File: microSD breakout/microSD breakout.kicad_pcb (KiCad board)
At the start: 2 copper layers, 17.1 x 17.8 mm, 4 parts, among them J1 Micro_SD_Card_Det_1Pin, J2 Conn_01x07

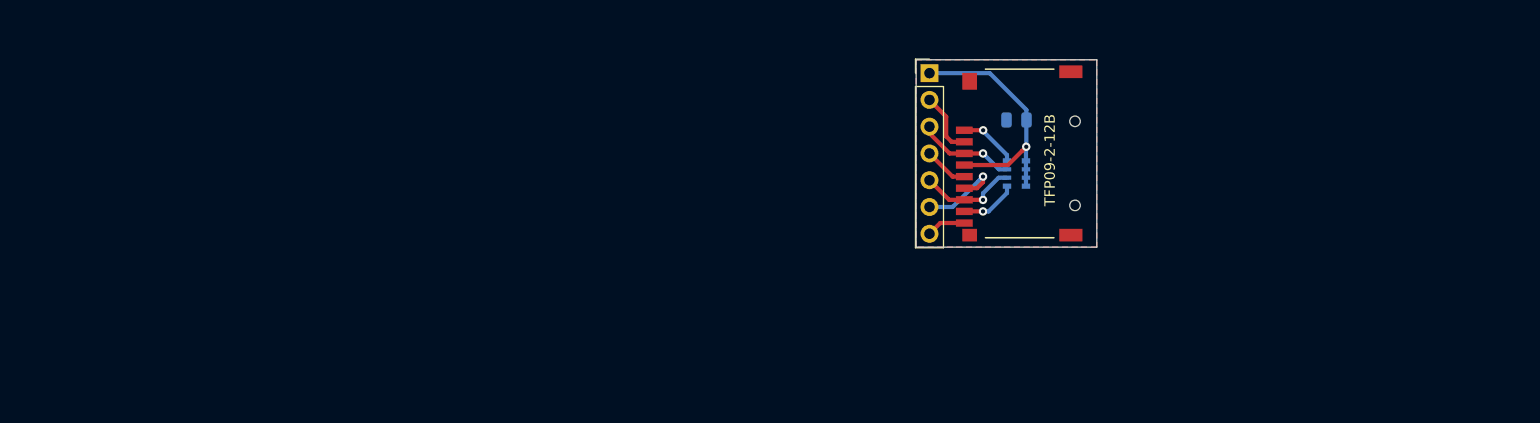
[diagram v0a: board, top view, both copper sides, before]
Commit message: Addition of 'microSD breakout' which is in fact an extension cable adapter that may work with my PiStorm'X boards. Renamed the microSD SPI socket breakout as 'microSD socket breakout'.
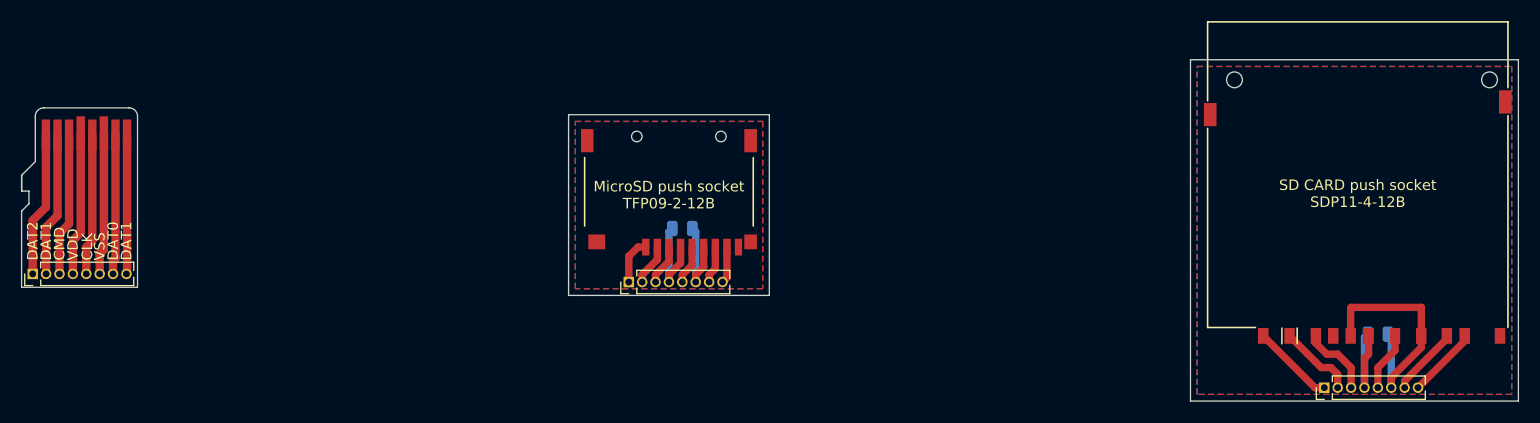
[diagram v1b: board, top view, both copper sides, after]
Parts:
- removed RN1: R_Pack04, Resistor_SMD:R_Array_Convex_4x0603
- added C2: C_Small, Capacitor_SMD:C_0805_2012Metric, B.Cu at (209.6, 115.6)
- added J3: Micro_SD_Card, Sassa:Micro_SD, F.Cu at (83.2, 96.7)
- added J4: Conn_01x08, Connector_PinHeader_1.27mm:PinHeader_1x08_P1.27mm_Vertical, F.Cu at (81.9, 109.9)
- added J5: SD_Card, Sassa:Conn_SDcard, F.Cu at (207.6, 91.4)
- added J6: Conn_01x08, Connector_PinHeader_1.27mm:PinHeader_1x08_P1.27mm_Vertical, F.Cu at (204.5, 120.7)
- J1: value Micro_SD_Card_Det_1Pin -> Conn_01x08; footprint Sassa:TFP09-2-12B -> Connector_PinHeader_1.27mm:PinHeader_1x08_P1.27mm_Vertical
- J2: value Conn_01x07 -> Micro_SD_Card_Det_1Pin; footprint Connector_PinHeader_2.54mm:PinHeader_1x07_P2.54mm_Vertical -> Sassa:TFP09-2-12B
- moved J1 34.6 mm to (138.5, 110.6)
- moved C1 33.3 mm to (143.6, 105.5), turned to 0 degrees
- moved J2 29.5 mm to (142.3, 106.8), turned to 180 degrees
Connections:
- net /SPI_CS renamed /SOCK_DAT3
- net /SPI_MOSI renamed /SOCK_CMD
- C1 pad 1: +3.3V -> /SOCK_VDD
- C1 pad 2: GND -> /SOCK_VSS
- J1 pad 1: Net-(J1-Pad1) -> /SOCK_DAT2
- J1 pad 4: +3.3V -> /SOCK_VDD
- J1 pad 5: /SPI_CLK -> /SOCK_CLK
- J1 pad 6: GND -> /SOCK_VSS
- J1 pad 7: /SPI_MISO -> /SOCK_DAT0
- J1 pad 8: Net-(J1-Pad8) -> /SOCK_DAT1
- J2 pad 1: +3.3V -> /SOCK_DAT2
- J2 pad 4: /SPI_CLK -> /SOCK_VDD
- J2 pad 5: /SPI_MISO -> /SOCK_CLK
- J2 pad 6: GND -> /SOCK_VSS
- J2 pad 7: /SD_DETECT -> /SOCK_DAT0
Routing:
- net +3.3V: track 24.5 -> 0.00 mm, vias 1 -> 0
- net /SOCKSD_VSS: track 0.00 -> 23.4 mm
- net /SD_DAT2: track 0.00 -> 13.7 mm
- net /SD_VDD: track 0.00 -> 13.7 mm
- net /SD_DAT3: track 0.00 -> 13.7 mm
- net /SD_CMD: track 0.00 -> 13.6 mm
- net /SD_VSS: track 0.00 -> 13.5 mm
- net /SD_CLK: track 0.00 -> 13.4 mm
- net /SD_DAT0: track 0.00 -> 13.3 mm
- net /SD_DAT1: track 0.00 -> 13.2 mm
- net /SOCKSD_VDD: track 0.00 -> 10.3 mm
- net /SPI_MISO: track 9.37 -> 0.00 mm, vias 1 -> 0
- net /SOCK_VDD: track 0.00 -> 8.98 mm
- net /SOCK_VSS: track 0.00 -> 8.84 mm
- net GND: track 8.81 -> 0.00 mm, vias 1 -> 0
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- added copper zone on B.Cu, net /SOCKSD_VSS
- added copper zone on F.Cu, net /SOCKSD_VSS
- added copper zone on B.Cu, net /SOCK_VSS
- added copper zone on F.Cu, net /SOCK_VSS
- removed copper zone on B.Cu, net GND
- removed copper zone on F.Cu, net GND
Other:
- board size 17.1 x 17.8 mm -> 142 x 32.4 mm
- rule pad_to_mask_clearance: 0.051 -> 0
- board text added: "CMD"
- board text added: "DAT0"
- board text added: "DAT1"
- board text added: "DAT2"
- board text added: "MicroSD push socket TFP09-2-12B"
- board text added: "PCB thickness including contacts = 0.7mm"
- board text added: "Ribbon from an IDE cable may be suitable to connect the SD to the socket board"
- board text added: "SD CARD push socket SDP11-4-12B"
- board text added: "VDD"
- board text added: "VSS"
- board text added: "You may add your own mounting holes to the PBC before production"
- board text added: "microSD breakout FLACO 2023 github.com/f1ac0"
- board text removed: "3.3v"
- board text removed: "CS"
- board text removed: "Detect"
- board text removed: "GND"
- board text removed: "MISO"
- board text removed: "MOSI"
- board text removed: "TFP09-2-12B"
- board text removed: "microSD break-out"
